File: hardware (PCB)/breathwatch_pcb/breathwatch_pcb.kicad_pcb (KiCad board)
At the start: 2 copper layers, 7 parts, among them J1 Conn_01x08_Socket, J2 Conn_01x08_Socket, J3 Conn_01x04_Socket, J4 USB_A, Q1 AO3401A

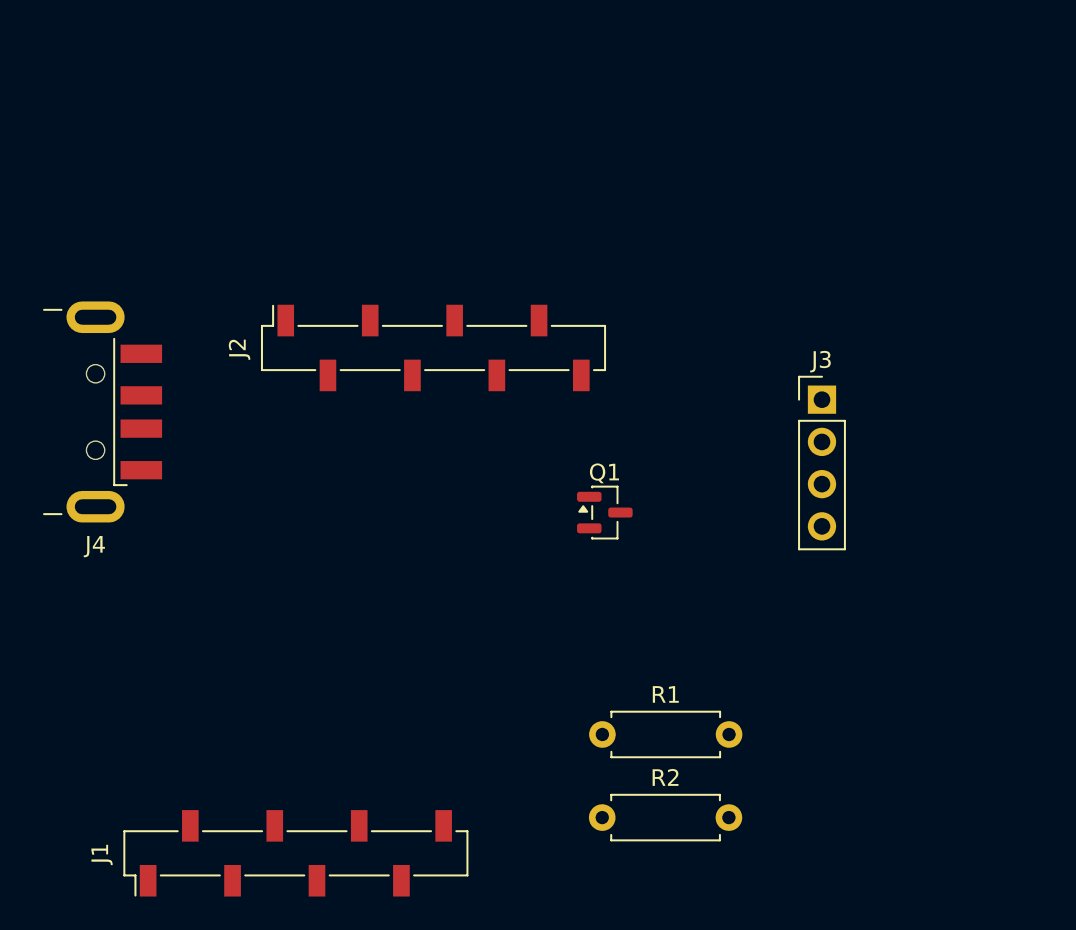
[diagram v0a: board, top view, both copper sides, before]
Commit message: added wiring
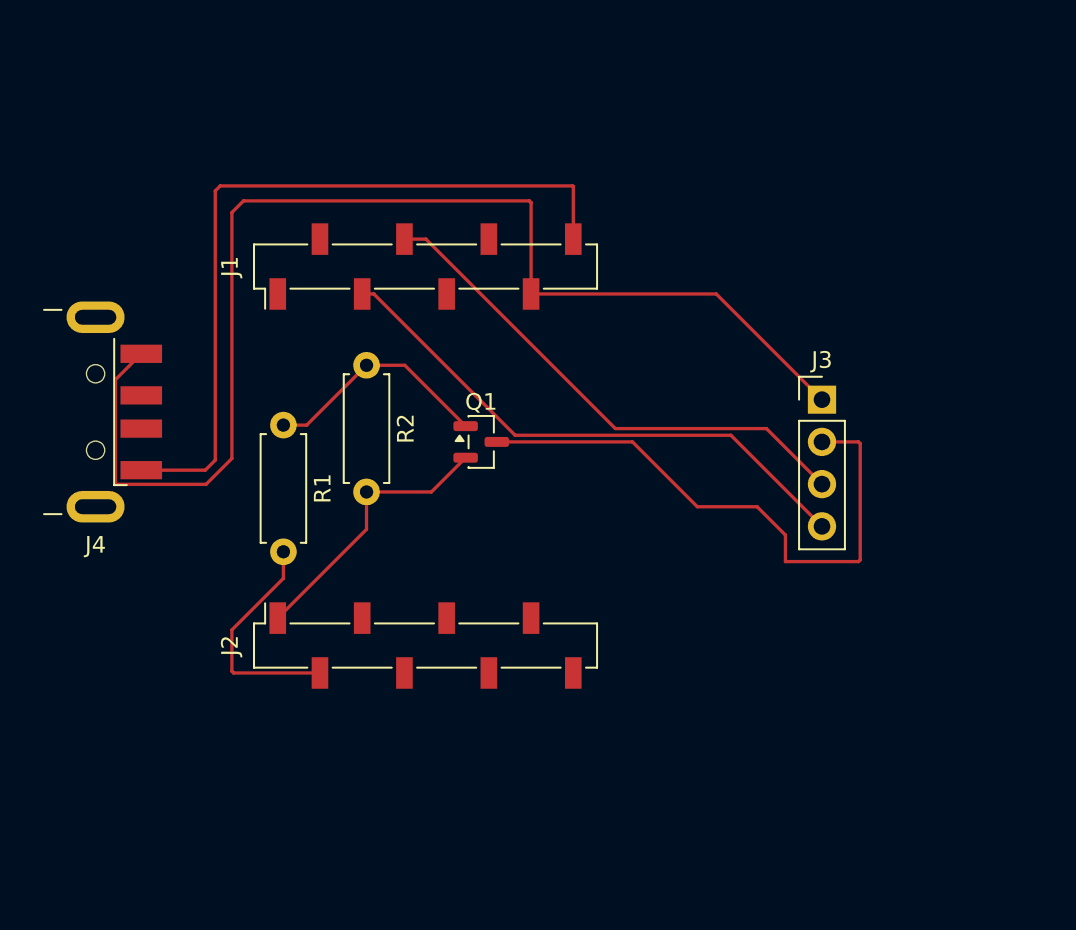
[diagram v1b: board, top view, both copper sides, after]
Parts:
- moved J1 36.2 mm to (103.8, 55.5)
- moved R2 30.7 mm to (100.3, 61.4), turned to -90 degrees
- moved R1 26.7 mm to (95.3, 65.0), turned to -90 degrees
- moved J2 17.9 mm to (103.8, 78.2)
- moved Q1 8.57 mm to (107.2, 66.0)
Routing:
- net GND: track 0.00 -> 74.9 mm
- net Net-(J1-Pin_8): track 0.00 -> 45.7 mm
- net Net-(J3-Pin_2): track 0.00 -> 35.2 mm
- net Net-(J1-Pin_3): track 0.00 -> 33.5 mm
- net Net-(J1-Pin_4): track 0.00 -> 31.2 mm
- net Net-(J2-Pin_1): track 0.00 -> 16.6 mm
- net Net-(Q1-G): track 0.00 -> 14.0 mm
- net Net-(J2-Pin_2): track 0.00 -> 13.8 mm

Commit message: added name
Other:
- board text added: "BreathWatch"
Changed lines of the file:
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@@
+		)
+	)
+	(gr_text "BreathWatch"
+		(at 100.6 73.6 0)
+		(layer "F.Cu")
+		(effects
+			(font
+				(size 1.5 1.5)
+				(thickness 0.3)
+				(bold yes)
+			)
+			(justify left bottom)
 		)
 	)

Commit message: fixed a few things (PCB, Schematic)
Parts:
- removed J3: Conn_01x04_Socket, Connector_PinHeader_2.54mm:PinHeader_1x04_P2.54mm_Vertical
- added J5: USB_C_Receptacle_PowerOnly_6P, Connector_USB:USB_C_Receptacle_GCT_USB4125-xx-x_6P_TopMnt_Horizontal, F.Cu at (81.9, 65.9)
- J4: value USB_A -> Conn_01x08_Socket; footprint Connector_USB:USB_A_CNCTech_1001-011-01101_Horizontal -> Connector_PinSocket_2.54mm:PinSocket_1x08_P2.54mm_Vertical_SMD_Pin1Right
- moved J4 61.1 mm to (137.9, 69.9), turned to 0 degrees
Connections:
- J4 pad 1: Net-(J1-Pin_8) -> unconnected-(J4-Pin_1-Pad1)
- J4 pad 2: unconnected-(J4-D--Pad2) -> Net-(J4-Pin_2)
- J4 pad 3: unconnected-(J4-D+-Pad3) -> GND
- J4 pad 4: GND -> Net-(J1-Pin_4)
- J4 pad 5: unconnected-(J4-Shield-Pad5) -> Net-(J1-Pin_3)
- Q1 pad 3: Net-(J3-Pin_2) -> Net-(J4-Pin_2)
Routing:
- net Net-(J4-Pin_2): track 0.00 -> 45.5 mm
- net Net-(J3-Pin_2): track 35.2 -> 0.00 mm
- net Net-(J1-Pin_3): track 33.5 -> 60.1 mm
- net Net-(J1-Pin_4): track 31.2 -> 39.9 mm
- net GND: track 74.9 -> 80.5 mm
- net Net-(J1-Pin_8): track 45.7 -> 47.4 mm

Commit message: Fixed a bit (PCB)
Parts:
- moved J4 18.8 mm to (119.4, 66.9)
- moved J5 3.91 mm to (85.7, 66.9)
- moved Q1 0.95 mm to (106.9, 66.9)
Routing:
- net Net-(J1-Pin_3): track 60.1 -> 25.6 mm
- net GND: track 80.5 -> 48.1 mm
- net Net-(J1-Pin_4): track 39.9 -> 20.1 mm
- net Net-(J4-Pin_2): track 45.5 -> 27.3 mm
- net unconnected-(J5-SHIELD-PadS1): track 0.00 -> 16.2 mm
- net Net-(J1-Pin_8): track 47.4 -> 38.4 mm
- net Net-(J2-Pin_2): track 13.8 -> 9.90 mm
- net Net-(J2-Pin_1): track 16.6 -> 15.9 mm
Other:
- board outline added: 41.5 x 33.4 mm

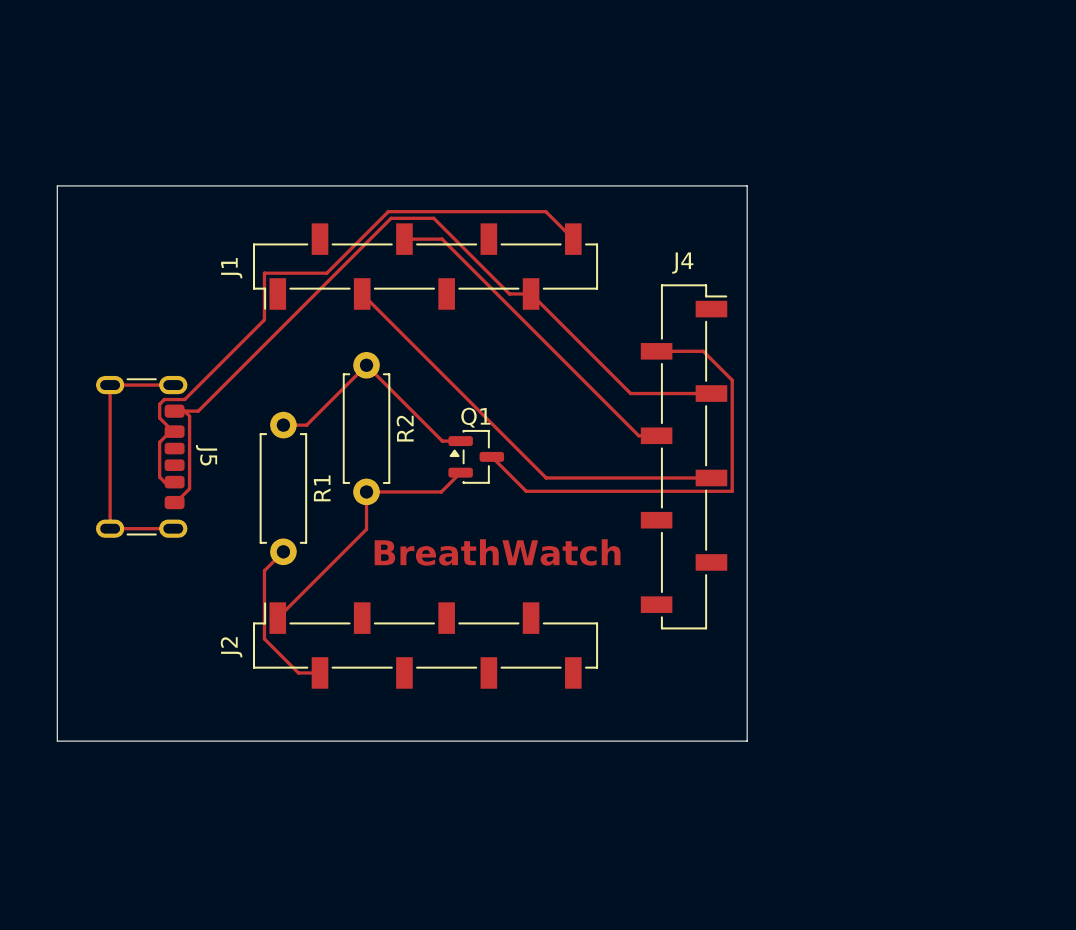
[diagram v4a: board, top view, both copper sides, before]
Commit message: added button to PCB
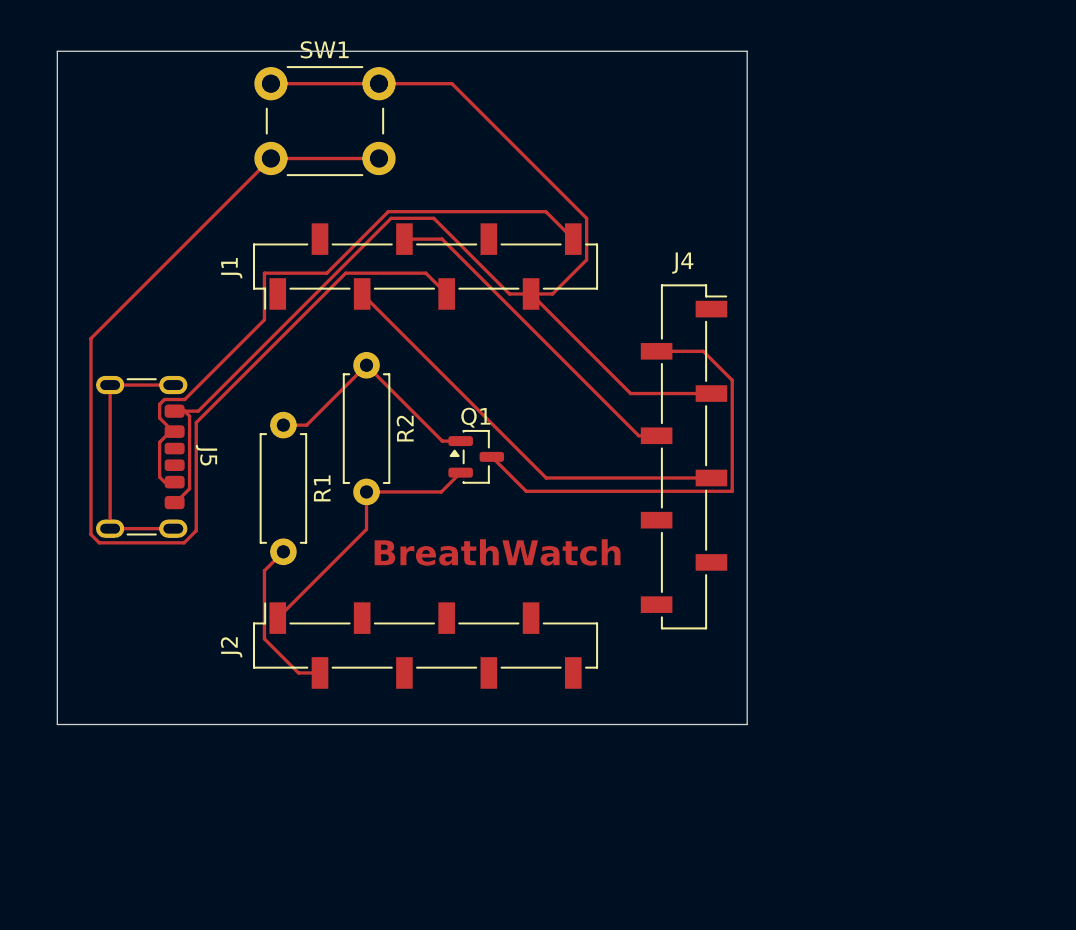
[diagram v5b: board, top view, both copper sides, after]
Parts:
- added SW1: SW_Push, Button_Switch_THT:SW_PUSH_6mm_H7.3mm, F.Cu at (94.5, 44.5)
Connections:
- J1 pad 5: unconnected-(J1-Pin_5-Pad5) -> Net-(J1-Pin_5)
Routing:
- net Net-(J1-Pin_5): track 0.00 -> 66.3 mm
- net GND: track 48.1 -> 77.1 mm
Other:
- board size 41.5 x 33.4 mm -> 41.5 x 40.5 mm

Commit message: fixed routing
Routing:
- net Net-(J1-Pin_5): track 66.3 -> 17.7 mm
- net GND: track 77.1 -> 67.6 mm, vias 0 -> 2
- net Net-(J4-Pin_2): track 27.3 -> 22.4 mm
- net Net-(J1-Pin_8): track 38.4 -> 41.2 mm, vias 0 -> 2
- net unconnected-(J5-SHIELD-PadS1): track 16.2 -> 18.5 mm
- net Net-(J1-Pin_3): track 25.6 -> 27.9 mm
- net Net-(J1-Pin_4): track 20.1 -> 20.8 mm
- net Net-(J2-Pin_2): track 9.90 -> 10.6 mm
- net Net-(Q1-G): track 14.0 -> 14.7 mm
